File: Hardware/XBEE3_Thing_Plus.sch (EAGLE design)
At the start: 43 parts, among them Q1 2.5A/30V, U1 XBEE3_Micro, U2 MCP73831, U3 AP2112K-3.3V, U4 CP2102N

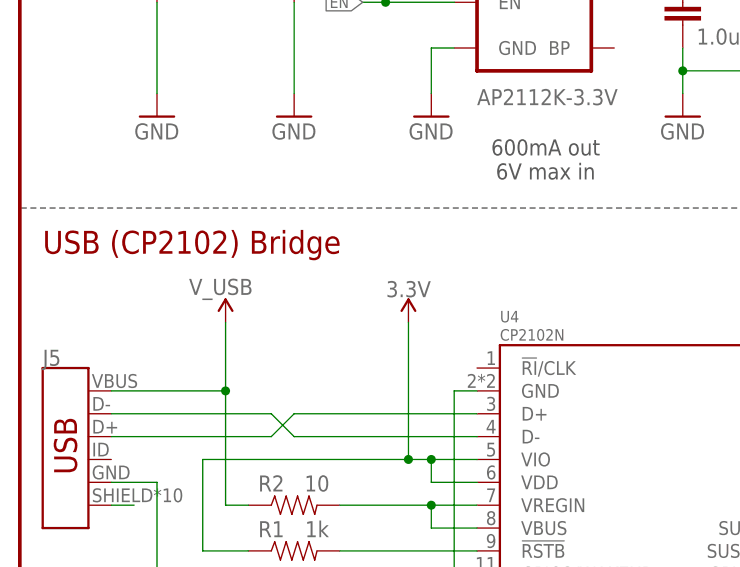
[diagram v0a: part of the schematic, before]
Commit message: Updated USB to UART bridge
Update schematic to use either the CP2104 or CP2102N USB to UART bridge
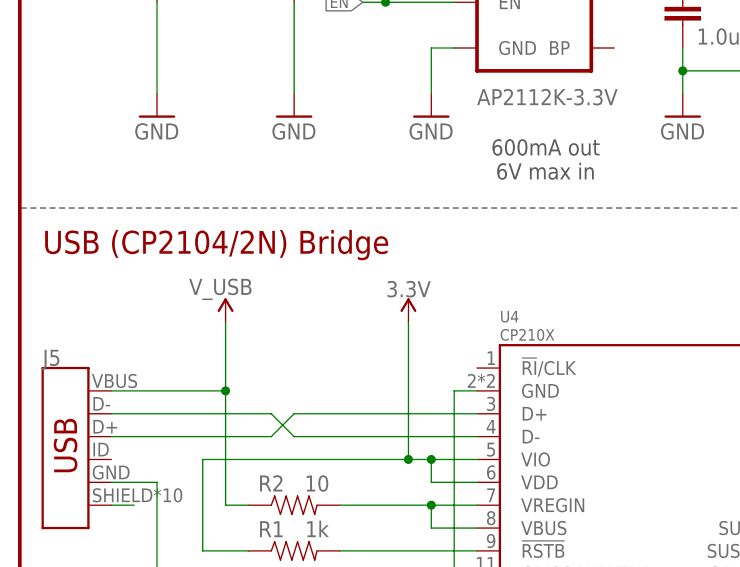
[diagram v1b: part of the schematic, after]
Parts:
- U4: value CP2102N -> CP210X
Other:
- note added: "USB (CP2104/2N) Bridge"
- note removed: "USB (CP2102) Bridge"
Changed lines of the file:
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@@
 <?xml version="1.0" encoding="utf-8"?>
 <!DOCTYPE eagle SYSTEM "eagle.dtd">
-<eagle version="9.4.1">
+<eagle version="9.5.2">
 <drawing>
 <settings>
-<setting alwaysvectorfont="no"/>
+<setting alwaysvectorfont="yes"/>
 <setting verticaltext="up"/>
 </settings>
@@
 <part name="GND26" library="SparkFun-Aesthetics" deviceset="GND" device=""/>
 <part name="SUPPLY14" library="SparkFun-Aesthetics" deviceset="V_USB" device=""/>
-<part name="U4" library="SparkFun-IC-Comms" deviceset="CP2102N" device=""/>
+<part name="U4" library="SparkFun-IC-Comms" deviceset="CP2102N" device="" value="CP210X"/>
 <part name="R1" library="SparkFun-Resistors" deviceset="1KOHM" device="-0603-1/10W-1%" value="1k"/>
 <part name="SUPPLY9" library="SparkFun-PowerSymbols" deviceset="3.3V" device=""/>
@@
 <wire x1="91.44" y1="185.42" x2="91.44" y2="111.76" width="0.1524" layer="97" style="shortdash"/>
 <wire x1="91.44" y1="111.76" x2="0" y2="111.76" width="0.1524" layer="97" style="shortdash"/>
-<text x="2.54" y="106.68" size="2.54" layer="94" font="vector">USB (CP2102) Bridge</text>
+<text x="2.54" y="106.68" size="2.54" layer="94" font="vector">USB (CP2104/2N) Bridge</text>
 <text x="187.96" y="180.34" size="2.54" layer="94" font="vector">Connectors</text>
 <text x="104.14" y="106.68" size="2.54" layer="94" font="vector">XBee3 Module</text>
